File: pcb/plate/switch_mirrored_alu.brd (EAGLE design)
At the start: 109 x 96 mm, 26 parts

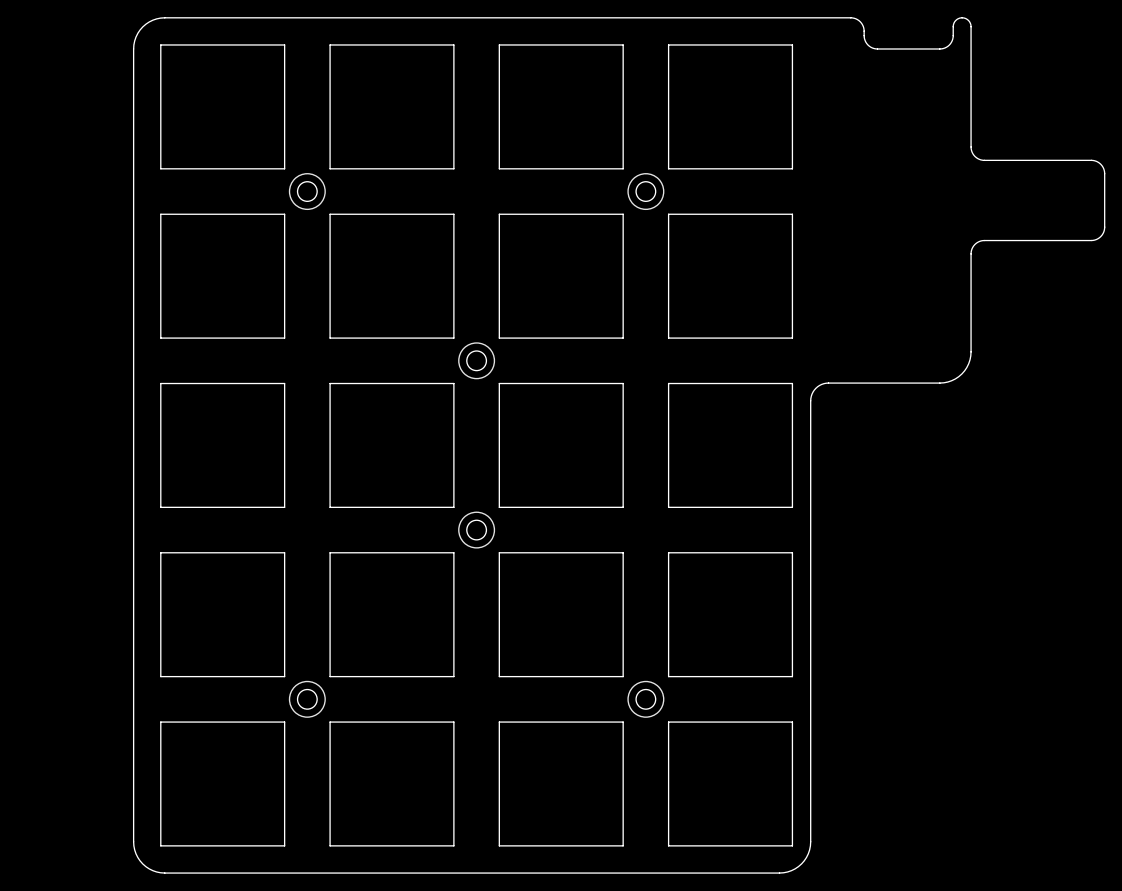
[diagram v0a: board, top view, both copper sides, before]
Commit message: updated plate material
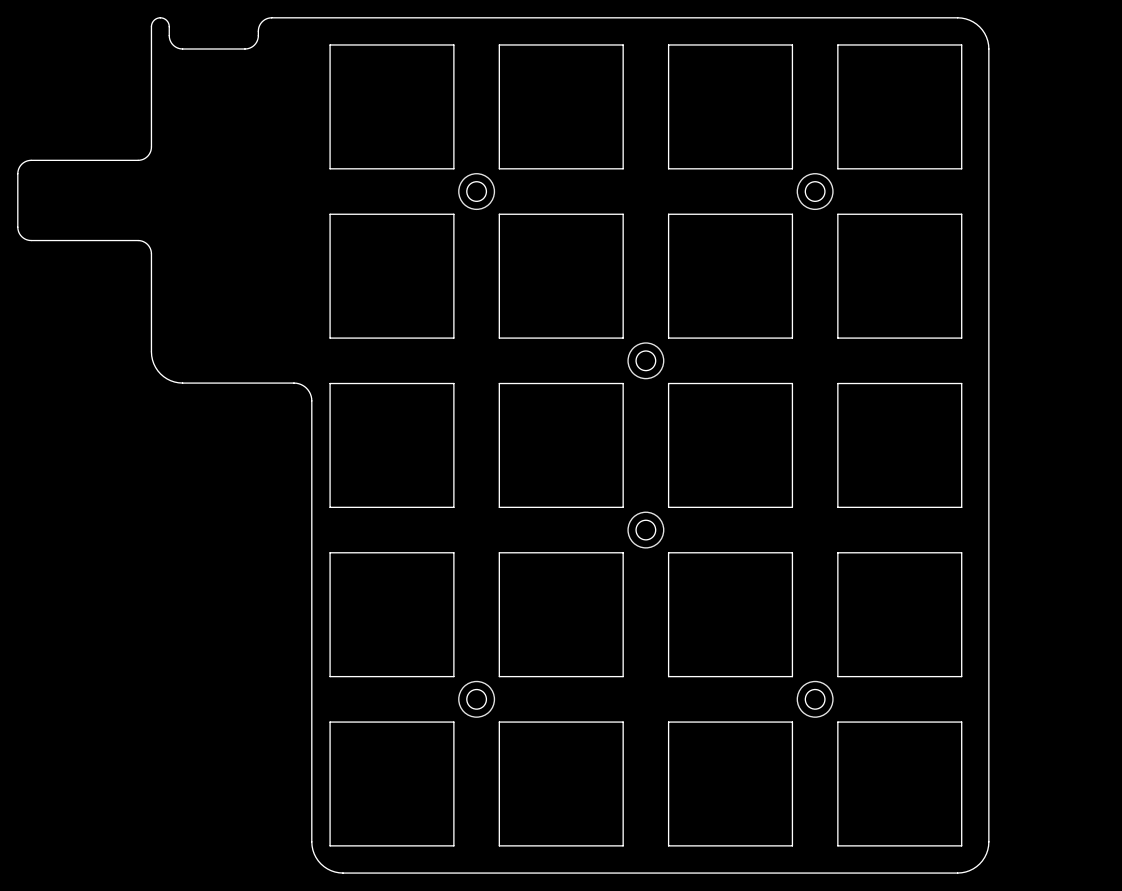
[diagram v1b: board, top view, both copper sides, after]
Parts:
- moved U$1 76.0 mm to (86.0, 10.0), flipped to the bottom
- moved U$11 76.0 mm to (86.0, 48.0), flipped to the bottom
- moved U$19 76.0 mm to (86.0, 67.0), flipped to the bottom
- moved U$20 76.0 mm to (86.0, 86.0), flipped to the bottom
- moved U$5 76.0 mm to (86.0, 29.0), flipped to the bottom
- moved U$14 57.0 mm to (76.5, 76.5), flipped to the bottom
- moved U$22 57.0 mm to (76.5, 19.5), flipped to the bottom
- moved U$10 38.0 mm to (29.0, 29.0), flipped to the bottom
- moved U$15 38.0 mm to (67.0, 48.0), flipped to the bottom
- moved U$18 38.0 mm to (29.0, 48.0), flipped to the bottom
- moved U$2 38.0 mm to (67.0, 10.0), flipped to the bottom
- moved U$21 38.0 mm to (67.0, 67.0), flipped to the bottom
- moved U$24 38.0 mm to (29.0, 67.0), flipped to the bottom
- moved U$25 38.0 mm to (67.0, 86.0), flipped to the bottom
- moved U$27 38.0 mm to (29.0, 86.0), flipped to the bottom
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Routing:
- removed copper zone on layer 2, net +3V3
- removed copper zone on layer 15, net GND
- removed copper zone on layer 15, net WTF2
- removed copper zone on layer 2, net WTF2
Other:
- outline, holes or cut-outs redrawn
